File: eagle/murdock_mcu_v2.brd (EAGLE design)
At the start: 47 x 31.8 mm, 31 parts, among them IC1 MPU-9150, IC2 LT1763CS8-3.3, IC3 STM32F4XX_64, U1 USD-SOCKETNEW, X1 USBSMD, X2 MURDOCK_STACK

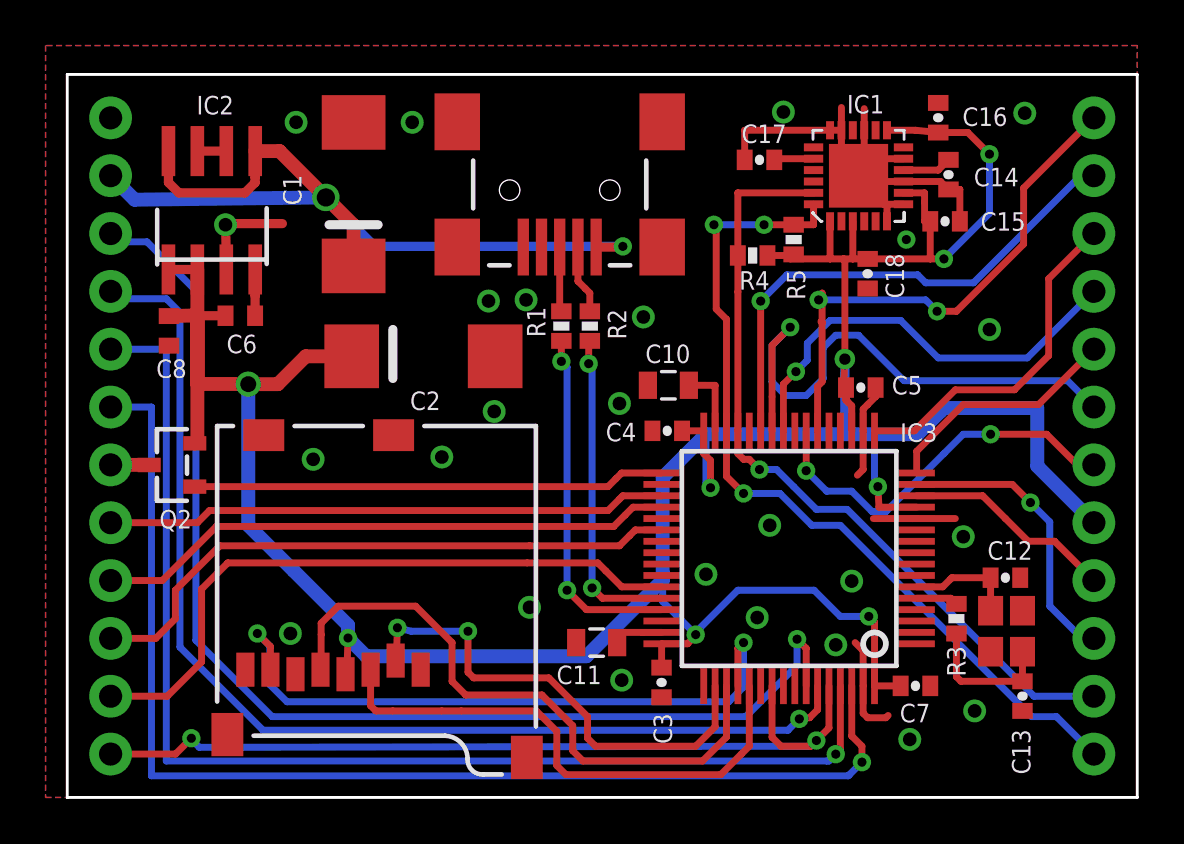
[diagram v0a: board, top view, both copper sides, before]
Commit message: updated labels
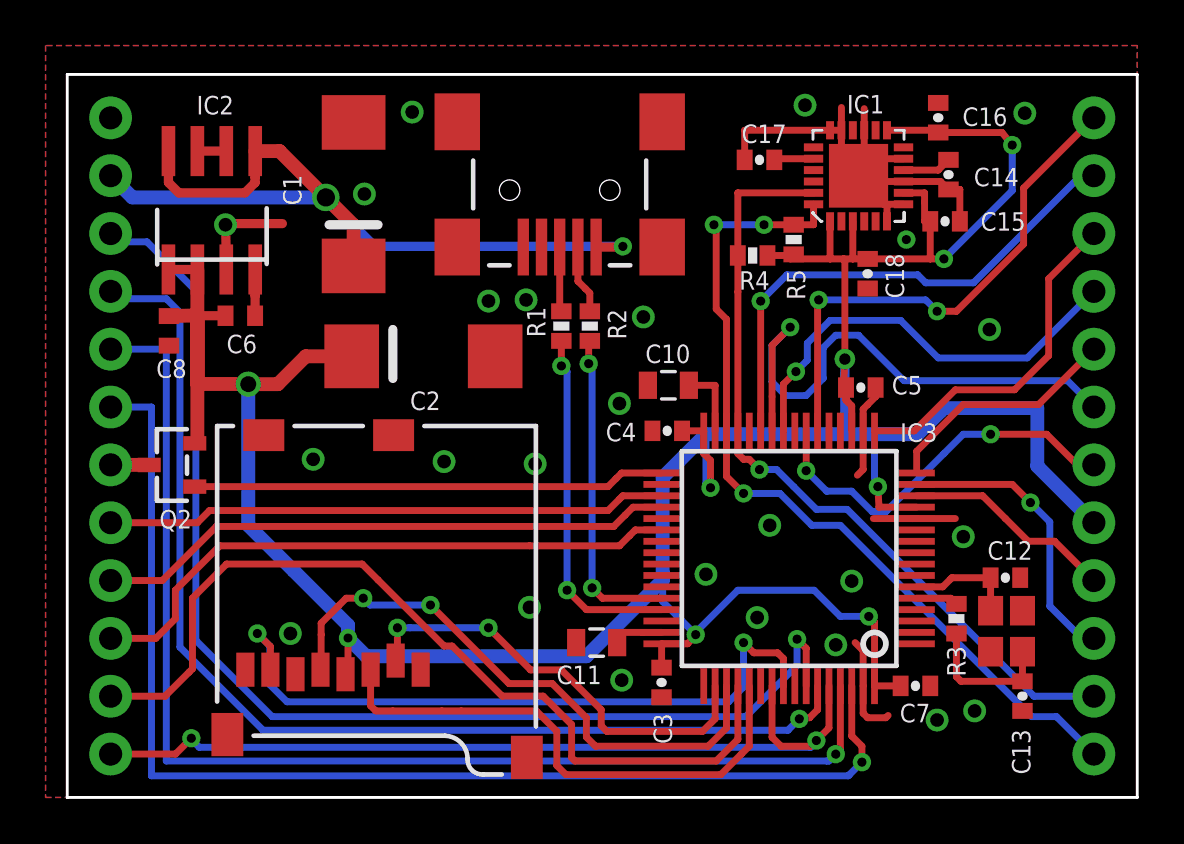
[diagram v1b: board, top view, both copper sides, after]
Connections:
- removed net A10: IC3.43, X2.SP1
- new net C11: IC3.52, X2.SP1
- net MISO: now also IC3.56; no longer IC3.52
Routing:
- net C11: track 0.00 -> 38.9 mm
- net A10: track 28.9 -> 0.00 mm
- net +3V3: track 152.6 -> 154.5 mm
- net SD_CS: track 21.3 -> 19.4 mm
- net SCK: track 27.3 -> 25.7 mm, vias 0 -> 2
- net MISO: track 29.6 -> 30.9 mm
- net PWM5: track 23.8 -> 23.0 mm
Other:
- board text added: "+"
- board text added: "-"
- board text added: "AUX"
- board text added: "GPS"
- board text added: "MURDOCK"
- board text added: "SBUS/PPM"
- board text added: "SP1"
- board text added: "SP2"
- board text added: "SRV1/THR"
- board text added: "SRV2/ELV"
- board text added: "SRV3/AIL1"
- board text added: "SRV4/AIL2"
- board text added: "SRV5/RUD"
- board text added: "SRV6"
- board text added: "SRV7"
- board text removed: "MUDOCK"

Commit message: smaller updates
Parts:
- added IC4: BMP085, SparkFun-Sensors:BMP085
- moved C1 10.8 mm to (20.1, 18.7), turned to 0 degrees
- moved C2 4.92 mm to (10.8, 18.6)
- moved R1 4.78 mm to (17.0, 21.6)
- moved R2 4.73 mm to (18.3, 21.6)
- moved X1 4.45 mm to (17.2, 26.6)
- moved U$1 0.60 mm to (17.1, 22.6)
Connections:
- net +3V3: now also IC4.3, IC4.4
- net GND: now also IC4.1
- net SCL: now also IC4.6
- net SDA: now also IC4.7
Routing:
- net +3V3: track 154.5 -> 171.4 mm
- net SCL: track 34.8 -> 43.0 mm, vias 1 -> 3
- net A12: track 15.6 -> 23.6 mm
- net A11: track 14.2 -> 18.6 mm
- net GND: track 41.4 -> 45.0 mm, vias 25 -> 27
- net SDA: track 37.7 -> 39.4 mm
- net N$1: track 3.04 -> 2.05 mm
- net N$2: track 2.85 -> 1.99 mm
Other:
- board text added: "IC4"
- board text added: "SRV1/AIL"
- board text added: "SRV3/THR"
- board text added: "SRV4/RUD"
- board text added: "SRV5/AIL2"
- board text added: "s"
- board text removed: "SRV1/THR"
- board text removed: "SRV3/AIL1"
- board text removed: "SRV4/AIL2"
- board text removed: "SRV5/RUD"

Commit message: updated stack schematic
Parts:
- moved X2 31.8 mm to (0.00, 0.00), turned to 0 degrees
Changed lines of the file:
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@@
 <attribute name="VALUE" x="15.4725" y="11.23" size="0.8128" layer="27" rot="R180"/>
 </element>
-<element name="X2" library="murdock" package="MURDOCK_STACK" value="MURDOCK_STACK" x="0" y="31.75" smashed="yes" rot="R270"/>
+<element name="X2" library="murdock" package="MURDOCK_STACK" value="MURDOCK_STACK" x="0" y="0" smashed="yes"/>
 <element name="IC2" library="linear-technology" package="SOIC8" value="LT1763CS8-3.3" x="6.35" y="25.785" smashed="yes">
 <attribute name="NAME" x="7.315" y="30.808" size="0.8128" layer="25" font="vector" ratio="10" rot="R180"/>

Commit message: values
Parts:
- C1: value (none) -> 47µF/10V
- C10, C11: value (none) -> 2.2µF
- C12, C13: value (none) -> 15pF
- C2: value (none) -> 100µF/6V
- C3, C4, C5, C7: value (none) -> 100nF
- L1: value (none) -> 12Mhz
- Q2: value (none) -> PFET
- R1, R2: value (none) -> 33R
- R3: value (none) -> 0R
- R4, R5: value (none) -> 4k7
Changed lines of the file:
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@@
 <attribute name="VALUE" x="4.7725" y="19.155" size="0.6096" layer="27" font="vector" ratio="10" rot="R90"/>
 </element>
-<element name="C1" library="rcl" package="SMC_D" value="" x="20.0925" y="18.7225" smashed="yes">
+<element name="C1" library="rcl" package="SMC_D" value="47µF/10V" x="20.0925" y="18.7225" smashed="yes">
 <attribute name="NAME" x="22.6525" y="20.4625" size="0.8128" layer="25" font="vector" ratio="10"/>
 <attribute name="VALUE" x="17.5525" y="14.9125" size="1.016" layer="27"/>
 </element>
-<element name="C2" library="rcl" package="SMC_D" value="" x="10.7925" y="18.5725" smashed="yes">
+<element name="C2" library="rcl" package="SMC_D" value="100µF/6V" x="10.7925" y="18.5725" smashed="yes">
 <attribute name="NAME" x="13.3025" y="20.5125" size="0.8128" layer="25" font="vector" ratio="10"/>
 <attribute name="VALUE" x="8.2525" y="14.7625" size="1.016" layer="27"/>
 </element>
-<element name="C3" library="SparkFun-Capacitors" package="0402-CAP" value="" x="26.1" y="5.05" smashed="yes" rot="R270">
+<element name="C3" library="SparkFun-Capacitors" package="0402-CAP" value="100nF" x="26.1" y="5.05" smashed="yes" rot="R270">
 <attribute name="NAME" x="25.7485" y="3.689" size="0.8128" layer="25" font="vector" ratio="10" rot="R270"/>
 <attribute name="VALUE" x="24.957" y="6.1295" size="0.4064" layer="27" rot="R270"/>
 </element>
-<element name="C4" library="SparkFun-Capacitors" package="0402-CAP" value="" x="26.35" y="16.1" smashed="yes" rot="R180">
+<element name="C4" library="SparkFun-Capacitors" package="0402-CAP" value="100nF" x="26.35" y="16.1" smashed="yes" rot="R180">
 <attribute name="NAME" x="25.189" y="16.8015" size="0.8128" layer="25" font="vector" ratio="10" rot="R180"/>
 <attribute name="VALUE" x="27.4295" y="17.243" size="0.4064" layer="27" rot="R180"/>
 </element>
-<element name="C5" library="SparkFun-Capacitors" package="0402-CAP" value="" x="34.85" y="18" smashed="yes">
+<element name="C5" library="SparkFun-Capacitors" package="0402-CAP" value="100nF" x="34.85" y="18" smashed="yes">
 <attribute name="NAME" x="36.211" y="17.6985" size="0.8128" layer="25" font="vector" ratio="10"/>
 <attribute name="VALUE" x="33.7705" y="16.857" size="0.4064" layer="27"/>
 </element>
-<element name="C7" library="SparkFun-Capacitors" package="0402-CAP" value="" x="37.25" y="4.9" smashed="yes">
+<element name="C7" library="SparkFun-Capacitors" package="0402-CAP" value="100nF" x="37.25" y="4.9" smashed="yes">
 <attribute name="NAME" x="36.561" y="3.2985" size="0.8128" layer="25" font="vector" ratio="10"/>
 <attribute name="VALUE" x="36.1705" y="3.757" size="0.4064" layer="27"/>
 </element>
-<element name="C10" library="SparkFun-Capacitors" package="0805" value="" x="26.4" y="18.1" smashed="yes">
+<element name="C10" library="SparkFun-Capacitors" package="0805" value="2.2µF" x="26.4" y="18.1" smashed="yes">
 <attribute name="NAME" x="25.388" y="19.0755" size="0.8128" layer="25" font="vector" ratio="10"/>
 <attribute name="VALUE" x="25.384" y="16.703" size="0.4064" layer="27"/>
 </element>
-<element name="C11" library="SparkFun-Capacitors" package="0805" value="" x="23.25" y="6.8" smashed="yes">
+<element name="C11" library="SparkFun-Capacitors" package="0805" value="2.2µF" x="23.25" y="6.8" smashed="yes">
 <attribute name="NAME" x="21.488" y="4.9755" size="0.8128" layer="25" font="vector" ratio="10"/>
 <attribute name="VALUE" x="22.234" y="5.403" size="0.4064" layer="27"/>
 </element>
-<element name="R1" library="SparkFun-Resistors" package="0402-RES" value="" x="17" y="21.55" smashed="yes" rot="R90">
+<element name="R1" library="SparkFun-Resistors" package="0402-RES" value="33R" x="17" y="21.55" smashed="yes" rot="R90">
 <attribute name="NAME" x="16.339" y="22.3015" size="0.8128" layer="25" font="vector" ratio="10" rot="R180"/>
 <attribute name="VALUE" x="18.143" y="20.4705" size="0.4064" layer="27" rot="R90"/>
 </element>
-<element name="R2" library="SparkFun-Resistors" package="0402-RES" value="" x="18.3" y="21.55" smashed="yes" rot="R90">
+<element name="R2" library="SparkFun-Resistors" package="0402-RES" value="33R" x="18.3" y="21.55" smashed="yes" rot="R90">
 <attribute name="NAME" x="20.489" y="22.3515" size="0.8128" layer="25" font="vector" ratio="10" rot="R180"/>
 <attribute name="VALUE" x="19.443" y="20.4705" size="0.4064" layer="27" rot="R90"/>
 </element>
-<element name="R3" library="SparkFun-Resistors" package="0402-RES" value="" x="39.05" y="7.85" smashed="yes" rot="R90">
+<element name="R3" library="SparkFun-Resistors" package="0402-RES" value="0R" x="39.05" y="7.85" smashed="yes" rot="R90">
 <attribute name="NAME" x="39.4515" y="5.311" size="0.8128" layer="25" font="vector" ratio="10" rot="R90"/>
 <attribute name="VALUE" x="40.193" y="6.7705" size="0.4064" layer="27" rot="R90"/>
 </element>
-<element name="C12" library="SparkFun-Capacitors" package="0402-CAP" value="" x="41.2" y="9.65" smashed="yes" rot="R180">
+<element name="C12" library="SparkFun-Capacitors" package="0402-CAP" value="15pF" x="41.2" y="9.65" smashed="yes" rot="R180">
 <attribute name="NAME" x="42.389" y="11.2515" size="0.8128" layer="25" font="vector" ratio="10" rot="R180"/>
 <attribute name="VALUE" x="42.2795" y="10.793" size="0.4064" layer="27" rot="R180"/>
 </element>
-<element name="C13" library="SparkFun-Capacitors" package="0402-CAP" value="" x="41.95" y="4.45" smashed="yes" rot="R90">
+<element name="C13" library="SparkFun-Capacitors" package="0402-CAP" value="15pF" x="41.95" y="4.45" smashed="yes" rot="R90">
 <attribute name="NAME" x="42.3015" y="1.011" size="0.8128" layer="25" font="vector" ratio="10" rot="R90"/>
 <attribute name="VALUE" x="43.093" y="3.3705" size="0.4064" layer="27" rot="R90"/>
 </element>
-<element name="L1" library="seb" package="X22" value="" x="41.25" y="7.3" smashed="yes" rot="R270"/>
-<element name="Q2" library="microbuilder" package="SOT23-R" value="" x="4.6" y="14.6" smashed="yes" rot="R90">
+<element name="L1" library="seb" package="X22" value="12Mhz" x="41.25" y="7.3" smashed="yes" rot="R270"/>
+<element name="Q2" library="microbuilder" package="SOT23-R" value="PFET" x="4.6" y="14.6" smashed="yes" rot="R90">
 <attribute name="NAME" x="5.472" y="12.627" size="0.8128" layer="25" font="vector" ratio="10" rot="R180"/>
 <attribute name="VALUE" x="5.235" y="16.378" size="0.4064" layer="27" ratio="10" rot="R90"/>
@@
 <attribute name="VALUE" x="31.4795" y="29.143" size="0.4064" layer="27" rot="R180"/>
 </element>
-<element name="R4" library="SparkFun" package="0402-RES" value="" x="30.1" y="23.8" smashed="yes">
+<element name="R4" library="SparkFun" package="0402-RES" value="4k7" x="30.1" y="23.8" smashed="yes">
 <attribute name="NAME" x="29.511" y="22.2985" size="0.8128" layer="25" font="vector" ratio="10"/>
 <attribute name="VALUE" x="29.0205" y="22.657" size="0.4064" layer="27"/>
 </element>
-<element name="R5" library="SparkFun" package="0402-RES" value="" x="31.9" y="24.5" smashed="yes" rot="R270">
+<element name="R5" library="SparkFun" package="0402-RES" value="4k7" x="31.9" y="24.5" smashed="yes" rot="R270">
 <attribute name="NAME" x="31.5985" y="23.189" size="0.8128" layer="25" font="vector" ratio="10" rot="R270"/>
 <attribute name="VALUE" x="30.757" y="25.5795" size="0.4064" layer="27" rot="R270"/>
